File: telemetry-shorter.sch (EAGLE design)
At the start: 60 parts, among them SW1 B3U-1000P-2P-SMD, U1 ATSAMD21G18_QFN, U2 SPX3819M5-L-3-0, U3 MCP73831T-2ACI/OT, U4 MPU-9250, U5 SIM868, U6 BMP280, X1 JSTPH, X2 32.768, X3 ZX62-B-5PA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

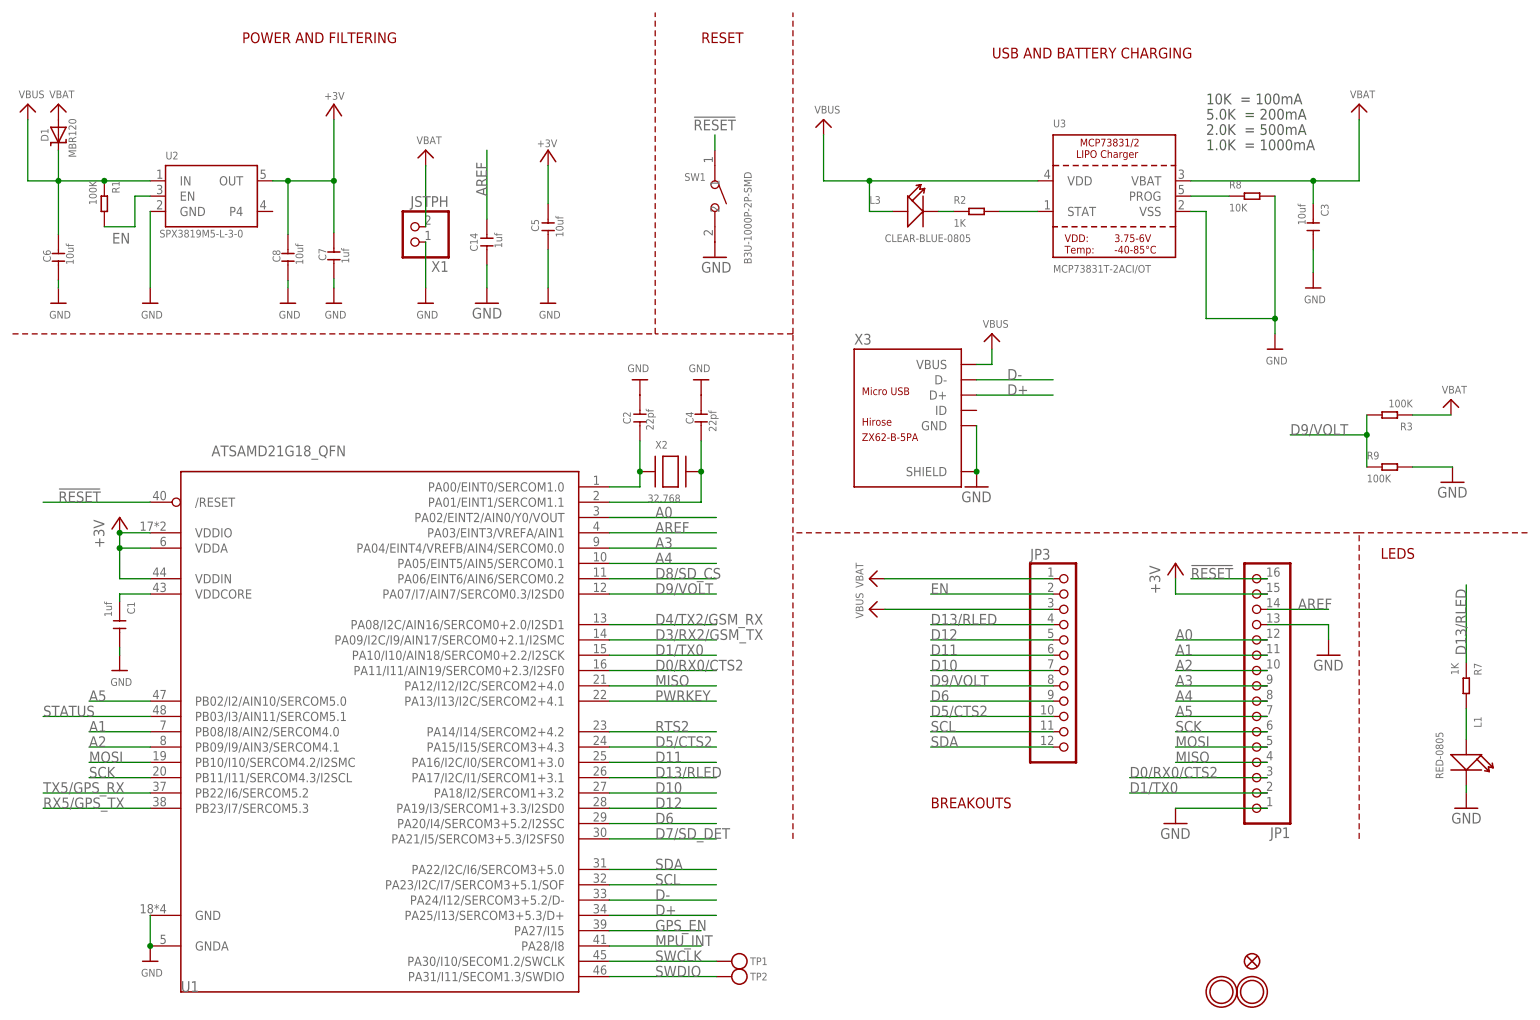
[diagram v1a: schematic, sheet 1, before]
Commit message: Updated for MacroFab
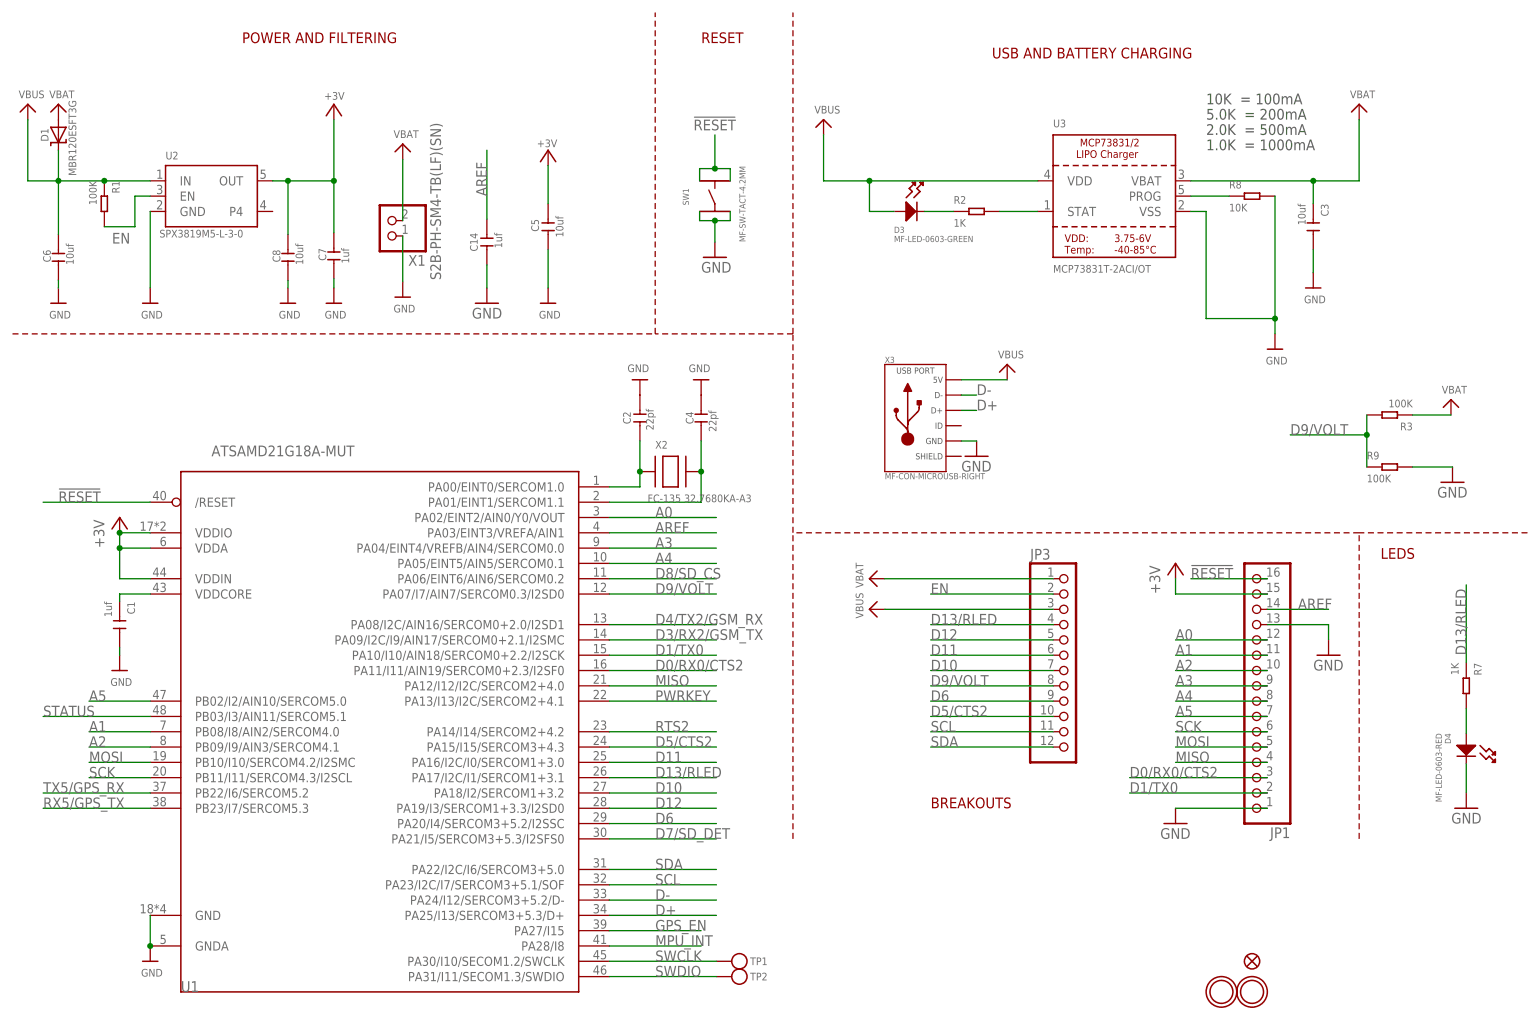
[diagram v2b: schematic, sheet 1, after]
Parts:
- removed L1: RED-0805, Seeed-LED-2016:SMD-LED-CLEAR-RED(0805)
- removed L3: CLEAR-BLUE-0805, Seeed-LED-2016:SMD-LED-CLEAR-BLUE(0805)
- added D3: MF-LED-0603-GREEN, MF_LEDs:LED_SINGLE-0603-GREEN
- added D4: MF-LED-0603-RED, MF_LEDs:LED_SINGLE-0603-RED
- D1: value MBR120 -> MBR120ESFT3G
- SW1: value B3U-1000P-2P-SMD -> MF-SW-TACT-4.2MM; device Seeed-Switch-2016:SMD-BUTTON(2P-3.0X2.5X1.2+0.4MM)-B3U-1000P-2P-SMD -> MF_Switches:TACT_4.2MM
- U1: value ATSAMD21G18_QFN -> ATSAMD21G18A-MUT
- X1: value JSTPH -> S2B-PH-SM4-TB(LF)(SN)
- X2: value 32.768 -> FC-135 32.7680KA-A3
- X3: value ZX62-B-5PA -> MF-CON-MICROUSB-RIGHT; device Deegou-Connectors:AO1SB141B1-067 -> MF_Connectors:USB_MICRO_RIGHT; SEEED ZX62-B-5PA -> (none)
- X5, X6: value U-FL -> U.FL-R-SMT(10)
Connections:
- net !RESET: now also SW1.P$1, SW1.P$2; no longer SW1.1
- net GND: now also D4.CATHODE, SW1.P$3, SW1.P$4; no longer L1.-, SW1.2, X3.SHIELD
- net N$1: now also D3.CATHODE; no longer L3.-
- net N$8: now also D4.ANODE; no longer L1.+
- net VBUS: now also D3.ANODE, X3.5V; no longer L3.+, X3.VBUS
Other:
- moved on the sheet: SW1, X1
